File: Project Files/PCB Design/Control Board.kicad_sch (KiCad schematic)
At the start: 42 parts, among them J1 Conn_01x04, J2 Conn_01x09, Q1 30V/60A Mosfet, Q2 2N3904, Q3 30V/60A Mosfet, Q5 2N3904, SW1 SW_SPST, SW2 SW_SPST, U1 ESP32-H2-DEVKITM-1-N4, U3 R-78E5.0-1.0

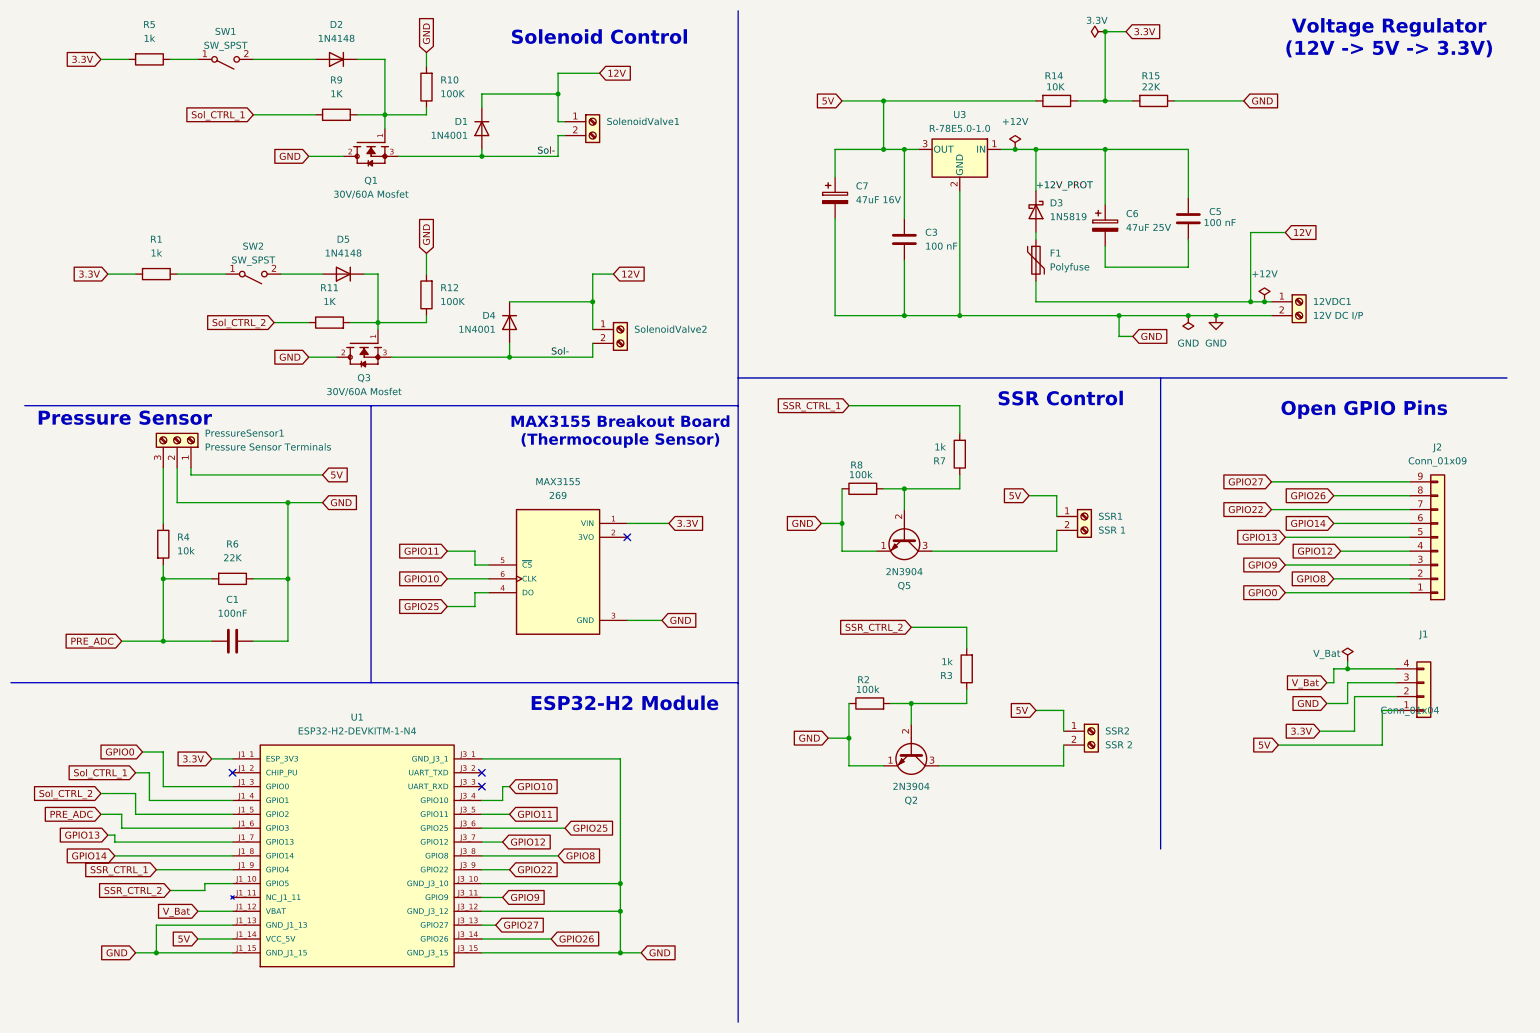
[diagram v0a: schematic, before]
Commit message: Add files via upload
Update schematic to v0.3.0
   
   - Updated component values
   - Verified all connections
   - Ready for PCB layout
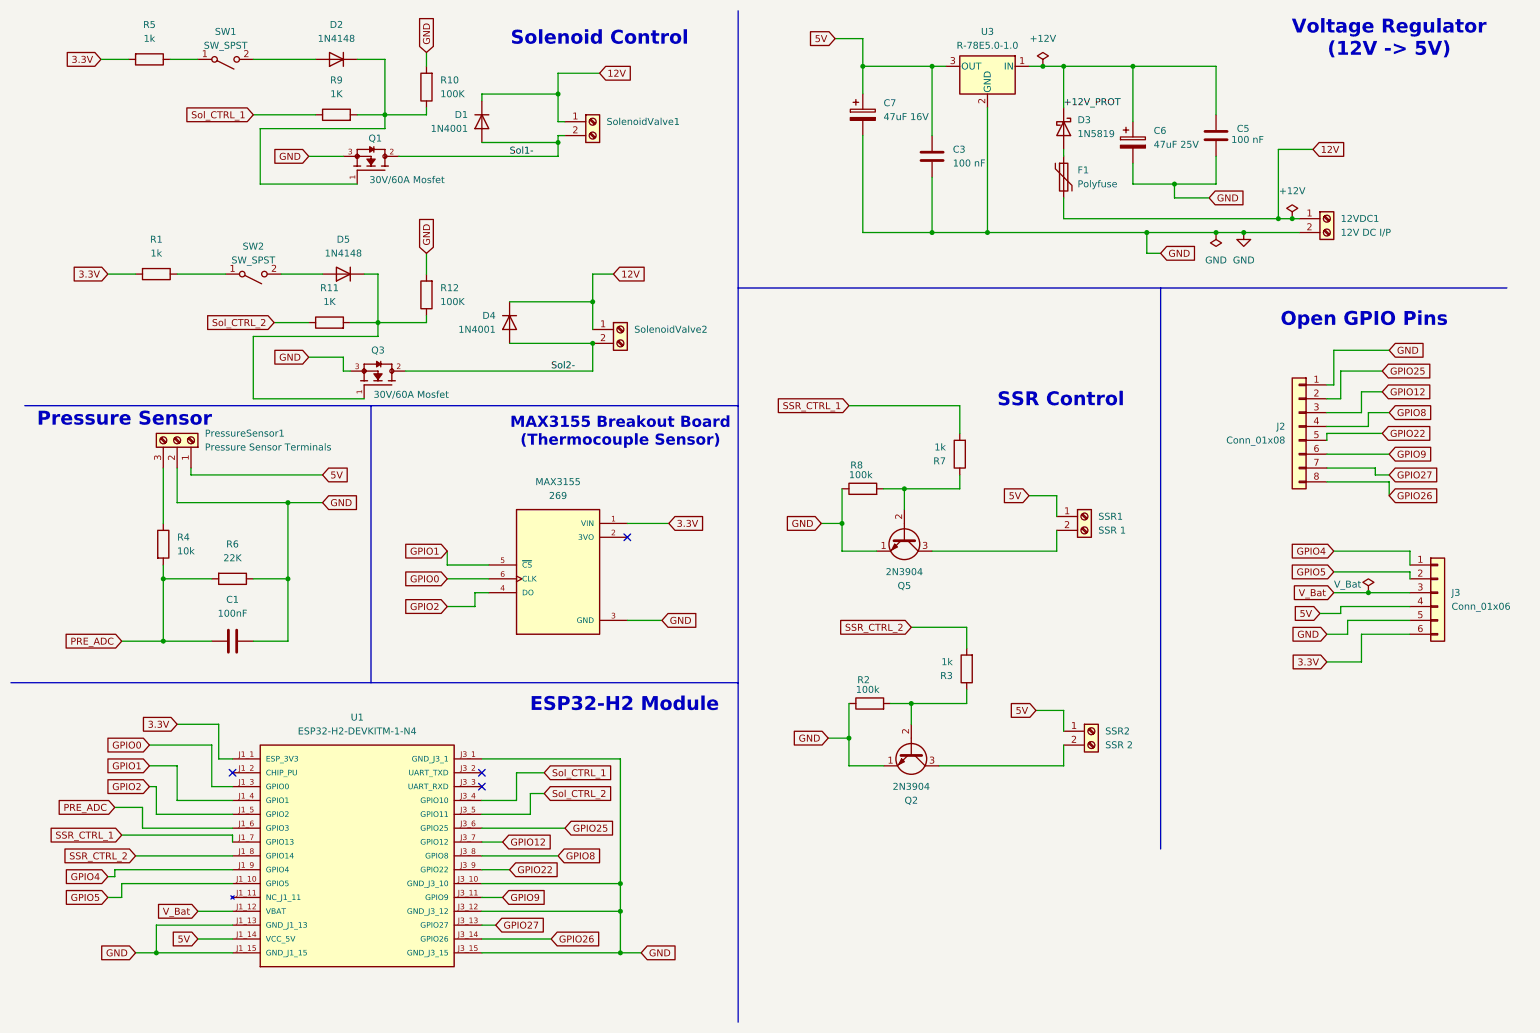
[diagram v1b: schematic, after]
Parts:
- removed J1: Conn_01x04, Connector_PinHeader_2.54mm:PinHeader_1x04_P2.54mm_Vertical, symbol Connector_Generic:Conn_01x04
- removed J2: Conn_01x09, Connector_PinHeader_2.54mm:PinHeader_1x09_P2.54mm_Vertical, symbol Connector_Generic:Conn_01x09
- removed R14: 10K, Resistor_THT:R_Axial_DIN0207_L6.3mm_D2.5mm_P7.62mm_Horizontal, symbol Device:R
- removed R15: 22K, Resistor_THT:R_Axial_DIN0207_L6.3mm_D2.5mm_P7.62mm_Horizontal, symbol Device:R
- added J2: Conn_01x08, Connector_PinHeader_2.54mm:PinHeader_1x08_P2.54mm_Vertical, symbol Connector_Generic:Conn_01x08
- added J3: Conn_01x06, Connector_PinHeader_2.54mm:PinHeader_1x06_P2.54mm_Vertical, symbol Connector_Generic:Conn_01x06
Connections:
- net GPIO13 is gone; now on net SSR_CTRL_1: U1.J1_7 (GPIO13)
- net GPIO14 is gone; now on net SSR_CTRL_2: U1.J1_8 (GPIO14)
- net 3.3V: now also J3.6 (Pin_6)
- net 5V: now also J3.4 (Pin_4)
- net GND: now also C5.2, C6.2, Q1.3, Q3.3, J2.1 (Pin_1), J3.5 (Pin_5); no longer Q1.2, Q3.2
- net GPIO0: now also MAX3155.6 (CLK)
- net GPIO12: now also J2.3 (Pin_3)
- net GPIO22: now also J2.5 (Pin_5)
- net GPIO25: now also J2.2 (Pin_2); no longer MAX3155.4 (DO)
- net GPIO26: now also J2.8 (Pin_8)
- net GPIO27: now also J2.7 (Pin_7)
- net GPIO8: now also J2.4 (Pin_4)
- net GPIO9: now also J2.6 (Pin_6)
- net SSR_CTRL_1: no longer U1.J1_9 (GPIO4)
- net SSR_CTRL_2: no longer U1.J1_10 (GPIO5)
- net Sol_CTRL_1: now also U1.J3_4 (GPIO10); no longer U1.J1_4 (GPIO1)
- net Sol_CTRL_2: now also U1.J3_5 (GPIO11); no longer U1.J1_5 (GPIO2)
- net V_Bat: now also J3.3 (Pin_3)
- removed net GPIO10: MAX3155.6 (CLK), U1.J3_4 (GPIO10)
- net GPIO11 renamed GPIO1
- net GPIO1: now also U1.J1_4 (GPIO1); no longer U1.J3_5 (GPIO11)
- removed net Sol-: D1.2 (A), D4.2 (A), Q1.3, Q3.3, SolenoidValve1.2 (Pin_2), SolenoidValve2.2 (Pin_2)
- new net GPIO2: MAX3155.4 (DO), U1.J1_5 (GPIO2)
- new net GPIO4: J3.1 (Pin_1), U1.J1_9 (GPIO4)
- new net GPIO5: J3.2 (Pin_2), U1.J1_10 (GPIO5)
- new net Sol1-: D1.2 (A), Q1.2, SolenoidValve1.2 (Pin_2)
- new net Sol2-: D4.2 (A), Q3.2, SolenoidValve2.2 (Pin_2)
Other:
- note added: "Voltage Regulator (12V -> 5V)"
- note removed: "Voltage Regulator (12V -> 5V -> 3.3V)"
- moved on the sheet: 12VDC1, C3, C5, C6, C7, D1, D3, F1, Q1, Q3, U3
